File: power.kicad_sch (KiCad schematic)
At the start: 40 parts, among them T1 net-tie, U2 TPS546D24ARVFR

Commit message: lots of misc
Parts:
- removed C14, C15, C16: 22uF, Capacitor_SMD:C_0805_2012Metric, symbol Device:C
- removed C6: 4700pF, Capacitor_SMD:C_0402_1005Metric, symbol Device:C
- removed C7: 1uF, Capacitor_SMD:C_0402_1005Metric, symbol Device:C
- removed C9: 2200pF, Capacitor_SMD:C_0402_1005Metric, symbol Device:C
- C2: value 10uF -> 100uF; footprint Capacitor_SMD:C_0805_2012Metric -> Capacitor_SMD:C_1206_3216Metric; DK 1276-1096-1-ND -> 1276-1782-1-ND; PARTNO CL21A106KOQNNNE -> CL31A107MQHNNNE
- C3, C4: value 47uF -> 100uF; footprint Capacitor_SMD:C_1210_3225Metric -> Capacitor_SMD:C_1206_3216Metric; DK 1276-3376-1-ND -> 1276-1782-1-ND; PARTNO CL32A476KOJNNNE -> CL31A107MQHNNNE
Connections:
- net 5V: no longer C2.1
- net VOUT: now also C2.1

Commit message: inductor change
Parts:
- L1: footprint bitaxe:SLC1175-271MEC_COC -> Inductor_SMD:L_Sunlord_MWSA1003S; Mouser 994-SLC1175-271MEC -> (none); PARTNO SLC1175-301MEC -> 104CDMCCDS-R30MC
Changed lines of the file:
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@@
 		(on_board yes)
 		(dnp no)
+		(fields_autoplaced yes)
 		(property "Reference" "L1"
-			(at 156.845 37.465 90)
+			(at 160.02 34.29 90)
 			(effects
 				(font
@@
 		)
 		(property "Value" "300nH"
-			(at 166.37 37.465 90)
+			(at 160.02 36.83 90)
 			(effects
 				(font
@@
 			)
 		)
-		(property "Footprint" "bitaxe:SLC1175-271MEC_COC"
+		(property "Footprint" "Inductor_SMD:L_Sunlord_MWSA1003S"
 			(at 160.02 39.37 0)
 			(effects
@@
 			)
 		)
-		(property "Datasheet" "https://www.mouser.com/datasheet/2/597/slc1175-270653.pdf"
+		(property "Datasheet" "https://products.sumida.com/products/pdf/104CDMCCDS.pdf"
 			(at 160.02 39.37 0)
 			(effects
@@
 			)
 		)
-		(property "Description" ""
+		(property "Description" "Inductor"
 			(at 160.02 39.37 0)
 			(effects
@@
 			)
 		)
-		(property "PARTNO" "SLC1175-301MEC"
+		(property "PARTNO" "104CDMCCDS-R30MC"
 			(at 160.02 39.37 90)
 			(effects
@@
 			)
 		)
-		(property "DK" ""
-			(at 160.02 39.37 90)
+		(property "partnum" ""
+			(at 160.02 39.37 0)
 			(effects
 				(font
-					(size 1.27 1.27)
-				)
-				(hide yes)
-			)
-		)
-		(property "Mouser" "994-SLC1175-271MEC"
-			(at 160.02 39.37 90)
-			(effects
-				(font
-					(size 1.27 1.27)
-				)
-				(hide yes)
-			)
-		)
-		(property "HEIGHT" ""
-			(at 160.02 39.37 90)
-			(effects
-				(font

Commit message: layout
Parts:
- removed C10: 4.7uF, Capacitor_SMD:C_0402_1005Metric, symbol Device:C
- added C7, C9: 10uF, Capacitor_SMD:C_0603_1608Metric, symbol Device:C_Small
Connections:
- net 5V: now also C7.1
- net GND: now also C7.2, C9.2
- net at U2.28 (VDD5): now also C9.1
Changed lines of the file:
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@@
 	)
 	(junction
+		(at 59.69 34.29)
+		(diameter 0)
+		(color 0 0 0 0)
+	)
+	(junction
 		(at 146.05 39.37)
 		(diameter 0)
@@
 	)
 	(junction
+		(at 71.12 17.78)
+		(diameter 0)
+		(color 0 0 0 0)
+	)
+	(junction
 		(at 101.6 48.26)
 		(diameter 0)
@@
 	(wire
 		(pts
+			(xy 71.12 27.94) (xy 71.12 34.29)
+		)
+		(stroke
+			(width 0)
+			(type default)
+		)
+	)
+	(wire
+		(pts
 			(xy 59.69 17.78) (xy 59.69 21.59)
 		)
@@
 	(wire
 		(pts
-			(xy 101.6 66.04) (xy 101.6 64.77)
+			(xy 101.6 68.58) (xy 101.6 64.77)
 		)
 		(stroke
@@
 	(wire
 		(pts
+			(xy 71.12 17.78) (xy 101.6 17.78)
+		)
+		(stroke
+			(width 0)
+			(type default)
+		)
+	)
+	(wire
+		(pts
 			(xy 64.77 72.39) (xy 78.74 72.39)
 		)
@@
 	(wire
 		(pts
+			(xy 71.12 17.78) (xy 71.12 22.86)
+		)
+		(stroke
+			(width 0)
+			(type default)
+		)
+	)
+	(wire
+		(pts
 			(xy 139.7 44.45) (xy 139.7 41.91)
 		)
@@
 	(wire
 		(pts
-			(xy 59.69 17.78) (xy 101.6 17.78)
+			(xy 59.69 17.78) (xy 71.12 17.78)
 		)
 		(stroke
@@
 	(wire
 		(pts
+			(xy 71.12 34.29) (xy 59.69 34.29)
+		)
+		(stroke
+			(width 0)
+			(type default)
+		)
+	)
+	(wire
+		(pts
 			(xy 153.67 81.28) (xy 153.67 76.2)
 		)
@@
 	)
 	(symbol
-		(lib_id "Device:C")
-		(at 101.6 69.85 0)
-		(unit 1)
-		(exclude_from_sim no)
-		(in_bom yes)
-		(on_board yes)
-		(dnp no)
-		(property "Reference" "C10"
-			(at 104.775 68.58 0)
-			(effects
-				(font
-					(size 1.27 1.27)
-				)
-				(justify left)
-			)
-		)
-		(property "Value" "4.7uF"
-			(at 104.775 71.12 0)
-			(effects
-				(font
-					(size 1.27 1.27)
-				)
-				(justify left)
-			)
-		)
-		(property "Footprint" "Capacitor_SMD:C_0402_1005Metric"
-			(at 102.5652 73.66 0)
-			(effects
-				(font
-					(size 1.27 1.27)
-				)
-				(hide yes)
-			)
-		)
-		(property "Datasheet" "~"
-			(at 101.6 69.85 0)
-			(effects
-				(font
-					(size 1.27 1.27)
-				)
-				(hide yes)
-			)
-		)
-		(property "Description" ""
-			(at 101.6 69.85 0)
-			(effects
-				(font
-					(size 1.27 1.27)
-				)
-				(hide yes)
-			)
-		)
-		(property "DK" "490-14306-1-ND"
-			(at 101.6 69.85 0)
-			(effects
-				(font
-					(size 1.27 1.27)
-				)
-				(hide yes)
-			)
-		)
-		(property "PARTNO" "GRM155R61A475MEAAD"
-			(at 101.6 69.85 0)
-			(effects
-				(font
-					(size 1.27 1.27)
-				)
-				(hide yes)
-			)
-		)
-		(pin "1"
-		)
-		(pin "2"
-		)
-		(instances
-			(project "bitaxeGamma"
-				(path "/e63e39d7-6ac0-4ffd-8aa3-1841a4541b55/8ec0a9c6-2b78-44ef-a83d-9047d2828409"
-					(reference "C10")
-					(unit 1)
-				)
-			)
-		)
-	)
-	(symbol
 		(lib_id "Connector:TestPoint")
 		(at 234.95 86.36 270)
@@
 	)
 	(symbol
+		(lib_id "Device:C_Small")
+		(at 101.6 71.12 0)
+		(unit 1)
+		(exclude_from_sim no)
+		(in_bom yes)
+		(on_board yes)
+		(dnp no)
+		(property "Reference" "C9"
+			(at 107.696 70.358 0)
+			(effects
+				(font
+					(size 1.27 1.27)
+				)
+				(justify right)
+			)
+		)
+		(property "Value" "10uF"
+			(at 107.696 72.644 0)
+			(effects
+				(font
+					(size 1.27 1.27)
+				)
+				(justify right)
+			)
+		)
+		(property "Footprint" "Capacitor_SMD:C_0603_1608Metric"
+			(at 101.6 71.12 0)
+			(effects
+				(font
+					(size 1.27 1.27)
+				)
+				(hide yes)
+			)
+		)
+		(property "Datasheet" "~"
+			(at 101.6 71.12 0)
+			(effects
+				(font
+					(size 1.27 1.27)
+				)
+				(hide yes)
+			)
+		)
+		(property "Description" "Unpolarized capacitor, small symbol"
+			(at 101.6 71.12 0)
+			(effects
+				(font
+					(size 1.27 1.27)
+				)
+				(hide yes)
+			)
+		)
+		(property "PARTNO" "GRM188R61E106KA73D"
+			(at 101.6 71.12 0)
+			(effects
+				(font
+					(size 1.27 1.27)
+				)
+				(hide yes)
+			)
+		)
+		(property "DK" "490-18214-1-ND"
+			(at 101.6 71.12 0)
+			(effects
+				(font
+					(size 1.27 1.27)
+				)
+				(hide yes)
+			)
+		)
+		(property "partnum" ""
+			(at 101.6 71.12 0)
+			(effects
+				(font
+					(size 1.27 1.27)
+				)
+				(hide yes)
+			)
+		)
+		(pin "1"
+		)
+		(pin "2"
+		)
+		(instances
+			(project "bitaxeGamma"
+				(path "/e63e39d7-6ac0-4ffd-8aa3-1841a4541b55/8ec0a9c6-2b78-44ef-a83d-9047d2828409"
+					(reference "C9")
+					(unit 1)
+				)
+			)
+		)
+	)
+	(symbol
 		(lib_id "Device:L")
 		(at 160.02 39.37 90)
@@
 					(unit 1)
 				)
+			)
+		)
+	)
+	(symbol
+		(lib_id "Device:C_Small")
+		(at 71.12 25.4 0)
+		(unit 1)
+		(exclude_from_sim no)
+		(in_bom yes)
+		(on_board yes)
+		(dnp no)
+		(property "Reference" "C7"
+			(at 77.216 24.638 0)
+			(effects
+				(font
+					(size 1.27 1.27)
+				)
+				(justify right)
+			)
+		)
+		(property "Value" "10uF"
+			(at 77.216 26.924 0)
+			(effects
+				(font
+					(size 1.27 1.27)
+				)
+				(justify right)
+			)
+		)
+		(property "Footprint" "Capacitor_SMD:C_0603_1608Metric"
+			(at 71.12 25.4 0)
+			(effects
+				(font
+					(size 1.27 1.27)
+				)
+				(hide yes)
+			)
+		)
+		(property "Datasheet" "~"
+			(at 71.12 25.4 0)
+			(effects
+				(font
+					(size 1.27 1.27)
+				)
+				(hide yes)
+			)
+		)
+		(property "Description" "Unpolarized capacitor, small symbol"
+			(at 71.12 25.4 0)
+			(effects
+				(font
+					(size 1.27 1.27)
+				)
+				(hide yes)
+			)
+		)
+		(property "PARTNO" "GRM188R61E106KA73D"
+			(at 71.12 25.4 0)
+			(effects
+				(font
+					(size 1.27 1.27)
+				)
+				(hide yes)
+			)
+		)
+		(property "DK" "490-18214-1-ND"
+			(at 71.12 25.4 0)
+			(effects
+				(font
+					(size 1.27 1.27)
+				)
+				(hide yes)
+			)
+		)
+		(property "partnum" ""
+			(at 71.12 25.4 0)
+			(effects
+				(font
+					(size 1.27 1.27)
+				)
+				(hide yes)
+			)
+		)
+		(pin "1"
+		)
+		(pin "2"
+		)
+		(instances
+			(project "bitaxeGamma"
+				(path "/e63e39d7-6ac0-4ffd-8aa3-1841a4541b55/8ec0a9c6-2b78-44ef-a83d-9047d2828409"
+					(reference "C7")
+					(unit 1)
+				)

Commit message: layout
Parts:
- L1: footprint Inductor_SMD:L_Sunlord_MWSA1003S -> bitaxe:SLC1175-271MEC_COC
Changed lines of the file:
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@@
 			)
 		)
-		(property "Footprint" "Inductor_SMD:L_Sunlord_MWSA1003S"
+		(property "Footprint" "bitaxe:SLC1175-271MEC_COC"
 			(at 160.02 39.37 0)
 			(effects

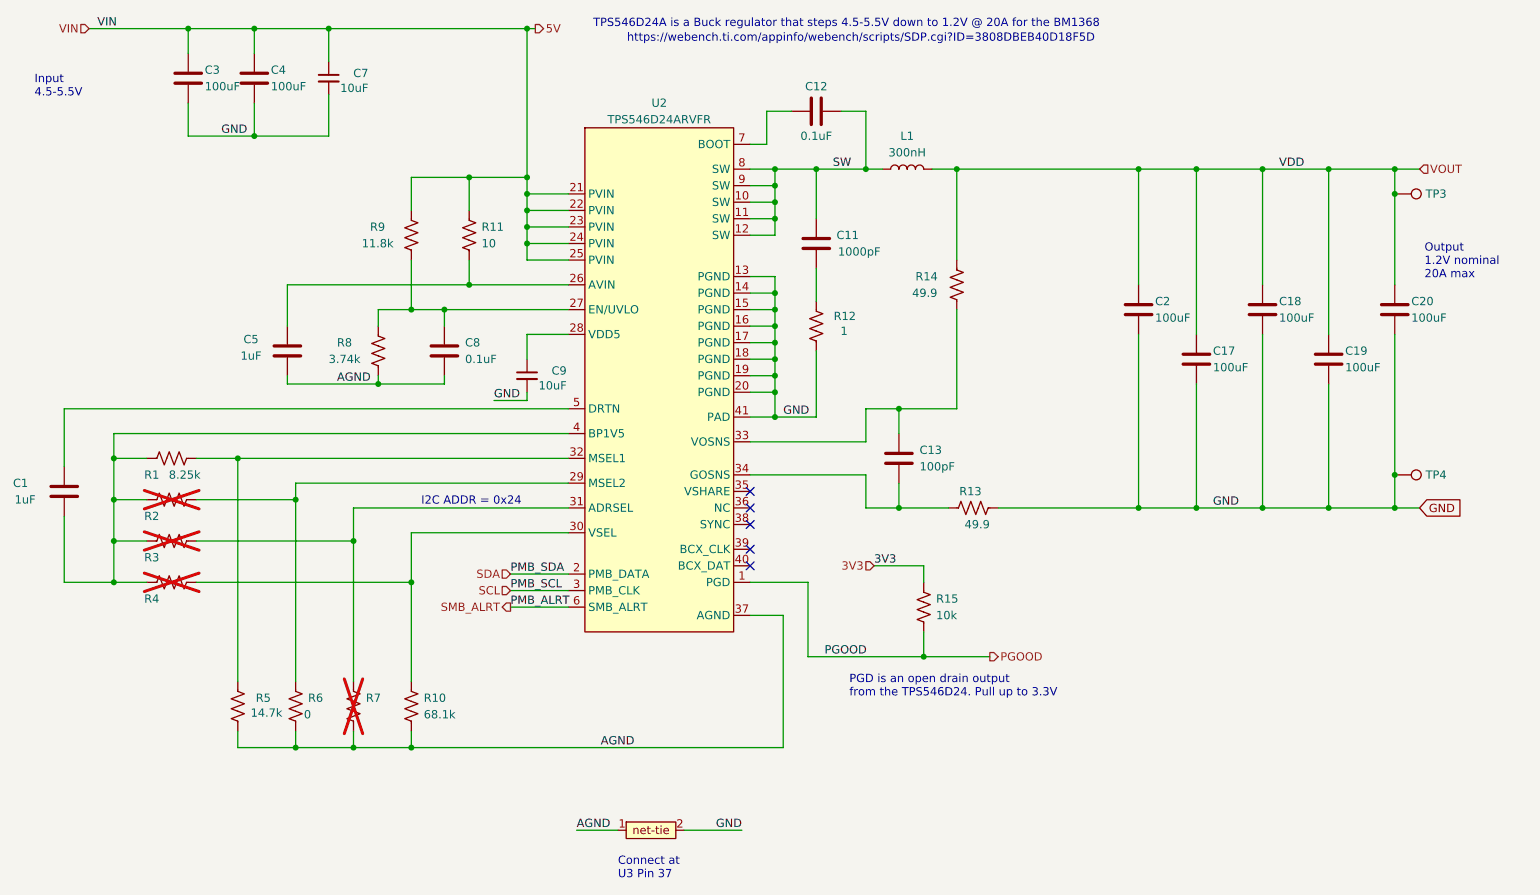
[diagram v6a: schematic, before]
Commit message: added pullup resistors for #25
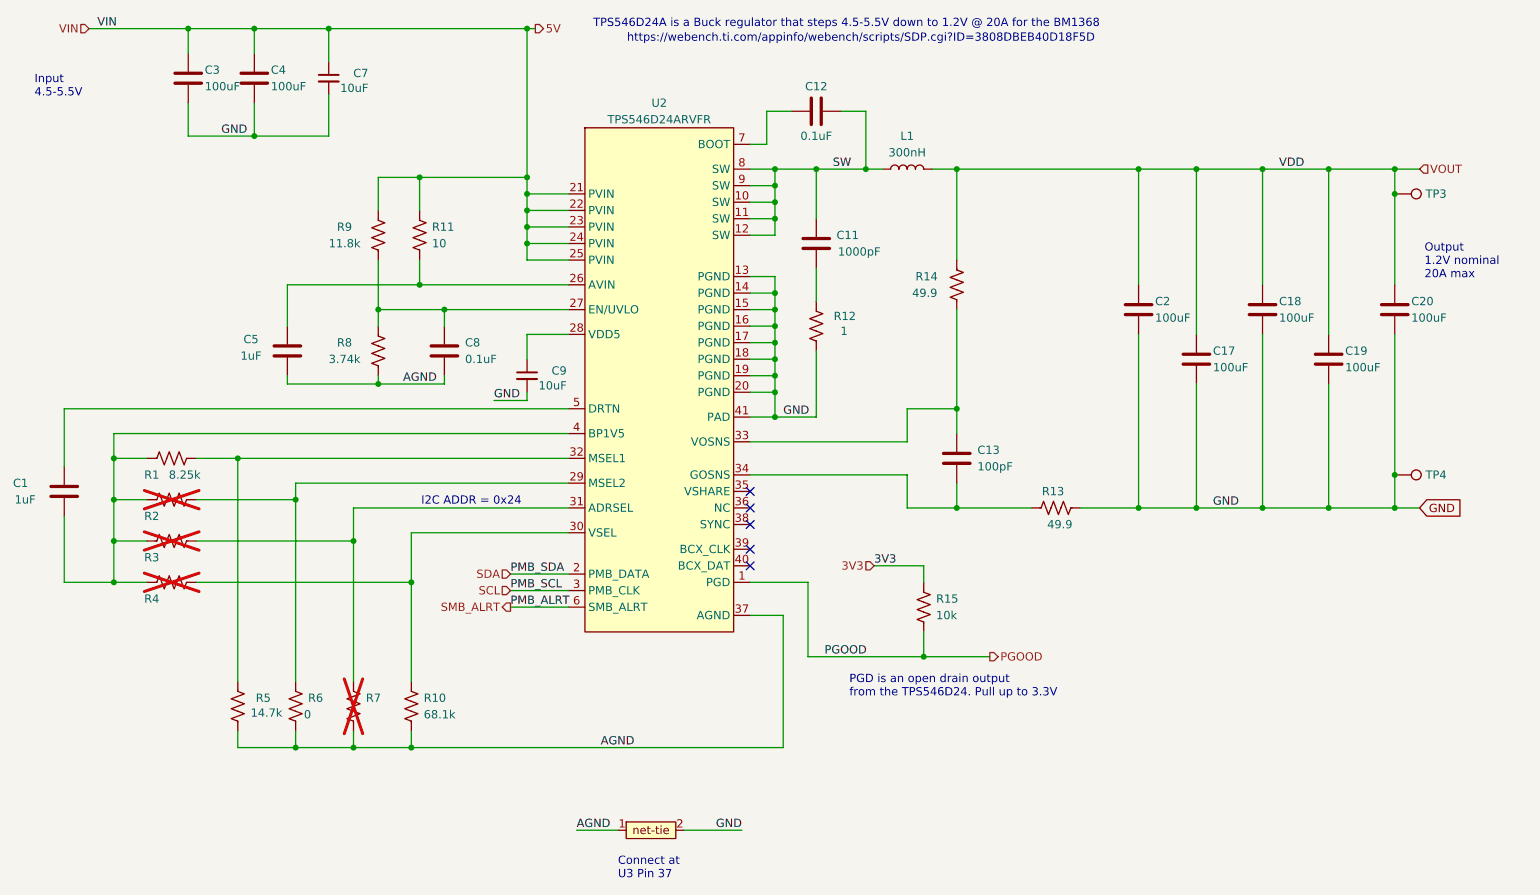
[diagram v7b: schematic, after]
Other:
- moved on the sheet: C13, R11, R13, R9

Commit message: update worksheet
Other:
- company: (none) -> bitaxeorg
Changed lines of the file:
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@@
 		(date "2025-04-29")
 		(rev "603")
+		(company "bitaxeorg")
+		(comment 1 "OHLv2")
 	)
 	(text "TPS546D24A is a Buck regulator that steps 4.5-5.5V down to 1.2V @ 20A for the BM1368"
